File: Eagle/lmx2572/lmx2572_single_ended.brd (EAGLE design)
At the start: 38 x 36 mm, 40 parts, among them X1 ECS-TXO-3225

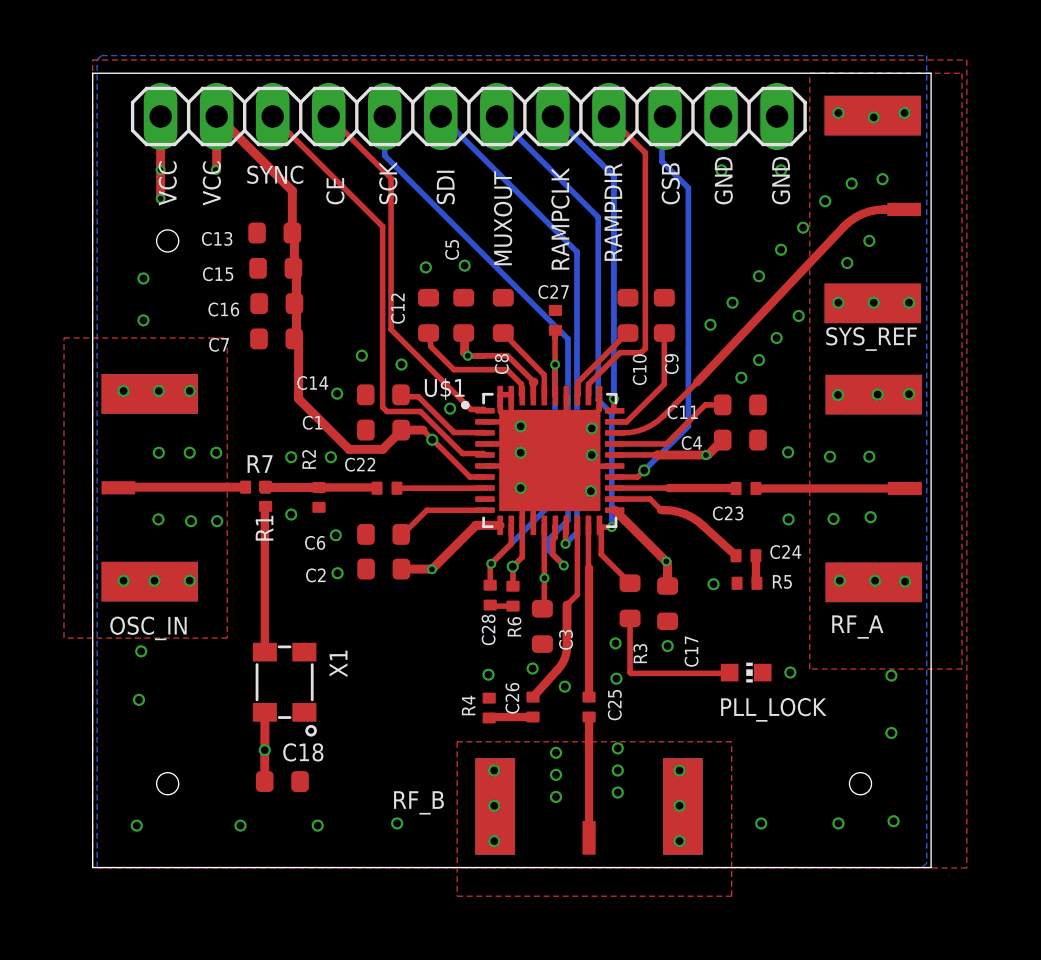
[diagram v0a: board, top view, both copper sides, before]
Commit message: removed thermal clearance.
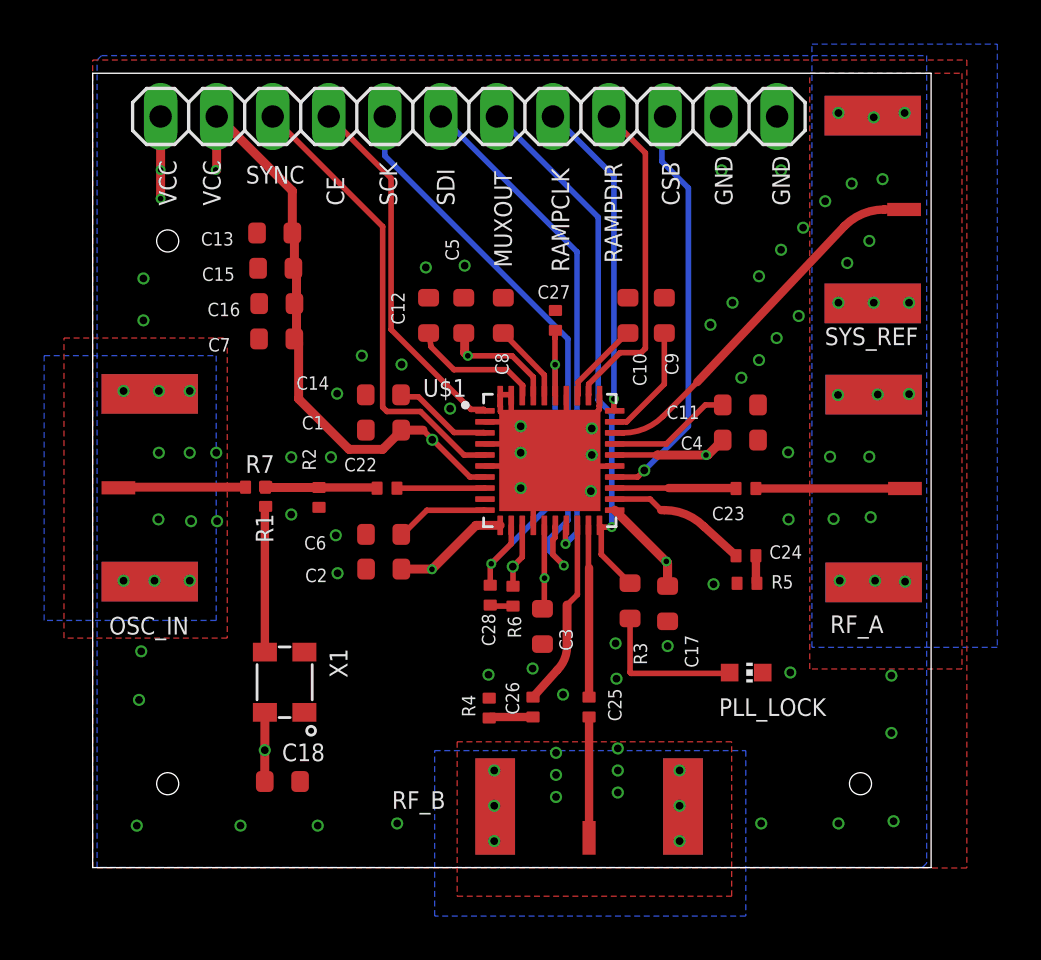
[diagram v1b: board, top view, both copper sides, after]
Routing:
- net GND: track 34.0 -> 32.7 mm
- net VCC: track 60.9 -> 60.2 mm
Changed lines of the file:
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@@
 <setting verticaltext="up"/>
 </settings>
-<grid distance="0.02" unitdist="mm" unit="mm" style="lines" multiple="5" display="yes" altdistance="2" altunitdist="mm" altunit="mm"/>
+<grid distance="0.01" unitdist="mm" unit="mm" style="lines" multiple="5" display="yes" altdistance="2" altunitdist="mm" altunit="mm"/>
 <layers>
 <layer number="1" name="Top" color="4" fill="1" visible="no" active="yes"/>
@@
 <layer number="14" name="Route14" color="22" fill="1" visible="no" active="no"/>
 <layer number="15" name="Route15" color="23" fill="1" visible="no" active="yes"/>
-<layer number="16" name="Bottom" color="1" fill="1" visible="yes" active="yes"/>
+<layer number="16" name="Bottom" color="1" fill="1" visible="no" active="yes"/>
 <layer number="17" name="Pads" color="2" fill="1" visible="yes" active="yes"/>
 <layer number="18" name="Vias" color="2" fill="1" visible="yes" active="yes"/>
@@
 <layer number="21" name="tPlace" color="7" fill="1" visible="no" active="yes"/>
 <layer number="22" name="bPlace" color="7" fill="1" visible="no" active="yes"/>
-<layer number="23" name="tOrigins" color="15" fill="1" visible="yes" active="yes"/>
-<layer number="24" name="bOrigins" color="15" fill="1" visible="yes" active="yes"/>
-<layer number="25" name="tNames" color="7" fill="1" visible="yes" active="yes"/>
-<layer number="26" name="bNames" color="7" fill="1" visible="yes" active="yes"/>
+<layer number="23" name="tOrigins" color="15" fill="1" visible="no" active="yes"/>
+<layer number="24" name="bOrigins" color="15" fill="1" visible="no" active="yes"/>
+<layer number="25" name="tNames" color="7" fill="1" visible="no" active="yes"/>
+<layer number="26" name="bNames" color="7" fill="1" visible="no" active="yes"/>
 <layer number="27" name="tValues" color="7" fill="1" visible="no" active="yes"/>
 <layer number="28" name="bValues" color="7" fill="1" visible="no" active="yes"/>
 <layer number="29" name="tStop" color="7" fill="3" visible="yes" active="yes"/>
 <layer number="30" name="bStop" color="7" fill="6" visible="no" active="yes"/>
-<layer number="31" name="tCream" color="7" fill="4" visible="yes" active="yes"/>
+<layer number="31" name="tCream" color="7" fill="4" visible="no" active="yes"/>
 <layer number="32" name="bCream" color="7" fill="5" visible="no" active="yes"/>
 <layer number="33" name="tFinish" color="6" fill="3" visible="no" active="yes"/>
@@
 <hole x="3.4" y="3.8" drill="1"/>
 <hole x="34.8" y="3.8" drill="1"/>
-<wire x1="12.8" y1="17.2" x2="0.6" y2="17.2" width="1.27" layer="29"/>
 <wire x1="22.6" y1="13.8" x2="22.6" y2="8.4" width="1.27" layer="29"/>
 <wire x1="22.6" y1="6.2" x2="22.6" y2="1" width="1.27" layer="29"/>
@@
 VCC - 3V3
 KG7ZVV</text>
+<wire x1="6.61" y1="17.21" x2="0.99" y2="17.21" width="1.27" layer="29"/>
 </plain>
 <attributes>
@@
 <class number="0" name="default" width="0.254" drill="0">
 </class>
-<class number="1" name="Power" width="0.4064" drill="0">
+<class number="1" name="Power" width="0" drill="0">
 </class>
 <class number="2" name="RF" width="0.38" drill="0">
@@
 <wire x1="26.76525" y1="2.8575" x2="26.7525" y2="2.766" width="0.254" layer="16"/>
 <wire x1="35.37775" y1="12.84925" x2="35.396" y2="12.9255" width="0.254" layer="16"/>
-<wire x1="18.57375" y1="18.57375" x2="18.57375" y2="18.8595" width="0.254" layer="1"/>
 <wire x1="18.97" y1="20.17775" x2="18.8448" y2="20.30295" width="0.254" layer="1"/>
 <wire x1="35.33775" y1="34.0995" x2="35.356" y2="34.0805" width="0.254" layer="16"/>
@@
 <via x="18.2" y="1.2" extent="1-16" drill="0.35"/>
 <via x="18.2" y="4.4" extent="1-16" drill="0.35"/>
-<via x="21.4" y="8.2" extent="1-16" drill="0.35"/>
+<via x="21.32" y="7.84" extent="1-16" drill="0.35"/>
 <via x="16.2" y="20.8" extent="1-16" drill="0.35"/>
 <via x="14" y="22.8" extent="1-16" drill="0.35"/>
@@
 <wire x1="18.51125" y1="21.43125" x2="18.95475" y2="21.43125" width="0.254" layer="1"/>
 <wire x1="19.97" y1="15.51" x2="19.97" y2="17.7" width="0.254" layer="1"/>
-<wire x1="19.47" y1="15.51" x2="19.47" y2="16.520925" width="0.254" layer="1"/>
 <wire x1="19.47" y1="16.520925" x2="19.579075" y2="16.520925" width="0.254" layer="1"/>
 <via x="28.5" y="31.6" extent="1-16" drill="0.35"/>
@@
 <vertex x="28.96" y="5.7"/>
 </polygon>
-<wire x1="19" y1="19.3" x2="18.57375" y2="18.8595" width="0" layer="19" extent="1-1"/>
-<wire x1="19.14525" y1="19.90725" x2="19" y2="19.3" width="0" layer="19" extent="1-1"/>
-<wire x1="19.2" y1="18.2" x2="19.4" y2="18.8" width="0" layer="19" extent="1-1"/>
+<polygon width="0.1524" layer="16" thermals="no">
+<vertex x="32.6" y="37.32"/>
+<vertex x="41" y="37.32"/>
+<vertex x="41" y="9.98"/>
+<vertex x="32.6" y="9.98"/>
+</polygon>
+<polygon width="0.1524" layer="16" thermals="no">
+<vertex x="15.5" y="5.3"/>
+<vertex x="29.6" y="5.3"/>
+<vertex x="29.6" y="-2.2"/>
+<vertex x="15.5" y="-2.2"/>
+</polygon>
+<polygon width="0.1524" layer="16" thermals="no">
+<vertex x="-2.2" y="23.2"/>
+<vertex x="5.6" y="23.2"/>
+<vertex x="5.6" y="11.2"/>
+<vertex x="-2.2" y="11.2"/>
+</polygon>
+<wire x1="19.4" y1="18.8" x2="19.2" y2="18.2" width="0" layer="19" extent="1-1"/>
+<wire x1="19" y1="19.3" x2="19.14525" y2="19.90725" width="0" layer="19" extent="1-1"/>
 </signal>
 <signal name="N$1">
@@
 <contactref element="U$1" pad="VREGVCO"/>
 <contactref element="C12" pad="1"/>
-<wire x1="19.431" y1="21.9075" x2="19.431" y2="21.43125" width="0.254" layer="1"/>
-<wire x1="18.77375" y1="22.56475" x2="19.431" y2="21.9075" width="0.254" layer="1"/>
+<wire x1="19.491" y1="21.8475" x2="19.491" y2="21.411" width="0.254" layer="1"/>
+<wire x1="18.77375" y1="22.56475" x2="19.491" y2="21.8475" width="0.254" layer="1"/>
 <wire x1="16.3735" y1="22.56475" x2="18.77375" y2="22.56475" width="0.254" layer="1"/>
 <wire x1="15.34364375" y1="23.59460625" x2="16.3735" y2="22.56475" width="0.254" layer="1"/>
-<wire x1="19.431" y1="21.43125" x2="19.47" y2="21.39" width="0.254" layer="1"/>
 <wire x1="15.34364375" y1="23.59460625" x2="15.224" y2="24.226" width="0.254" layer="1"/>
+<wire x1="19.491" y1="21.411" x2="19.47" y2="21.39" width="0" layer="19" extent="1-1"/>
 </signal>
 <signal name="N$6">
@@
 <wire x1="14.097" y1="13.62075" x2="13.992" y2="13.528" width="0.4064" layer="1"/>
 <wire x1="20.28825" y1="11.6205" x2="20.386" y2="11.728" width="0.4064" layer="1"/>
-<wire x1="17.0025" y1="23.19325" x2="17.76425" y2="23.19325" width="0.254" layer="1"/>
-<wire x1="18.812" y1="23.19325" x2="20.0025" y2="22.00275" width="0.254" layer="1"/>
-<wire x1="17.0025" y1="23.19325" x2="18.812" y2="23.19325" width="0.254" layer="1"/>
 <wire x1="16.85925" y1="24.09825" x2="16.818" y2="24.226" width="0.4064" layer="1"/>
 <wire x1="28.47975" y1="19.33575" x2="28.556" y2="19.374" width="0.4064" layer="1"/>
@@
 <wire x1="17.0025" y1="23.19325" x2="16.85925" y2="23.3365" width="0.4064" layer="1"/>
 <wire x1="16.85925" y1="23.3365" x2="16.85925" y2="24.09825" width="0.4064" layer="1"/>
-<wire x1="19.97" y1="21.39" x2="19.97" y2="21.97025" width="0.254" layer="1"/>
-<wire x1="19.97" y1="21.97025" x2="20.0025" y2="22.00275" width="0.4064" layer="1"/>
 <wire x1="15.4" y1="19.4" x2="15.38893125" y2="19.38893125" width="0.4064" layer="1"/>
 <via x="15.38893125" y="19.38893125" extent="1-16" drill="0.35"/>
@@
 <wire x1="27.7985" y1="18.696" x2="25.5985" y2="18.696" width="0.4064" layer="1"/>
 <wire x1="25.5985" y1="18.696" x2="25.5945" y2="18.7" width="0.4064" layer="1"/>
+<wire x1="19.97" y1="21.39" x2="19.97" y2="22.23" width="0.254" layer="1"/>
+<wire x1="19.00675" y1="23.19325" x2="17.0025" y2="23.19325" width="0.254" layer="1"/>
+<wire x1="19.97" y1="22.23" x2="19.00675" y2="23.19325" width="0.254" layer="1"/>
 </signal>
 <signal name="N$13" class="2">
@@
 <contactref element="U$1" pad="SYNC"/>
 <contactref element="JP1" pad="3"/>
-<wire x1="16.764" y1="18.76425" x2="17.7165" y2="18.76425" width="0.254" layer="1"/>
-<wire x1="14.859" y1="20.66925" x2="16.764" y2="18.76425" width="0.254" layer="1"/>
+<wire x1="14.859" y1="20.66925" x2="16.834" y2="18.69425" width="0.254" layer="1"/>
 <wire x1="13.335" y1="20.66925" x2="14.859" y2="20.66925" width="0.254" layer="1"/>
 <wire x1="13.1445" y1="20.85975" x2="13.335" y2="20.66925" width="0.254" layer="1"/>
 <wire x1="13.1445" y1="29.05125" x2="13.1445" y2="20.85975" width="0.254" layer="1"/>
 <wire x1="8.1915" y1="34.00425" x2="13.1445" y2="29.05125" width="0.254" layer="1"/>
-<wire x1="17.7165" y1="18.76425" x2="17.78" y2="18.7" width="0.254" layer="1"/>
 <wire x1="8.1915" y1="34.00425" x2="8.16" y2="34.04" width="0.254" layer="1"/>
+<wire x1="16.834" y1="18.69425" x2="17.77425" y2="18.69425" width="0.254" layer="1"/>
+<wire x1="17.78" y1="18.7" x2="17.77425" y2="18.69425" width="0.254" layer="1"/>
 </signal>
 <signal name="RAMPCLK">

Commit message: review and updates before sending it to oshpark
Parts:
- removed PLL_LOCK: (no value), led:CHIP-LED0603
- added PLL, PWR: (no value), led:CHIP-LED0603
- added R8: 0, oresat-rcl:.0402-C-NOSILK
- added R9: 330, oresat-rcl:.0603-B-NOSILK
- moved X1 1.47 mm to (8.75, 9.87)
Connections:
- new net N$10: R8.1, X1.4
- new net N$25: PWR.A, R9.1
- net GND: now also PLL.C, PWR.C; no longer PLL_LOCK.C
- net N$14: now also PLL.A; no longer PLL_LOCK.A
- net VCC: now also R8.2, R9.2; no longer X1.4
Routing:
- net VCC: track 60.2 -> 43.6 mm, vias 10 -> 12
- net N$25: track 0.00 -> 1.92 mm
- net N$10: track 0.00 -> 1.55 mm
- net N$9: track 6.62 -> 5.14 mm
- net GND: vias 97 -> 109
